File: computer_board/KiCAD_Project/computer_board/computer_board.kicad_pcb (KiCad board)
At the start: 4 copper layers, 101.6 x 33 mm, 43 parts, among them J1 Digitiziers, J2 Laser Driver, J3 Raspberry_Pi, Q1 BSS138, Q10 BSS138, Q11 BSS138, Q12 BSS138, Q2 BSS138, Q3 BSS138, Q4 BSS138, Q5 BSS138, Q6 BSS138, Q7 BSS138, Q8 BSS138, Q9 BSS138

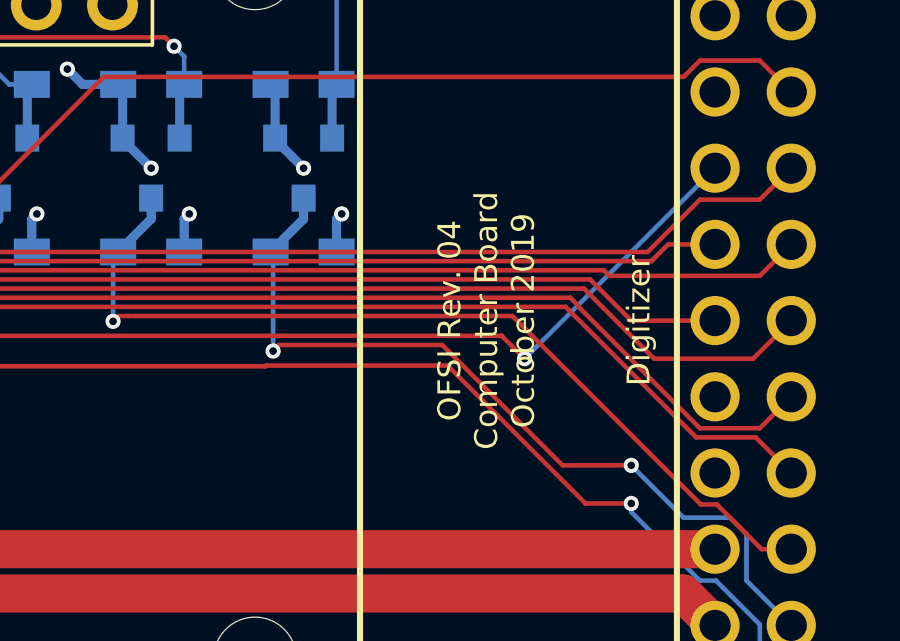
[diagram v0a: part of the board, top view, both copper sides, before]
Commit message: Change computer board to OFMI
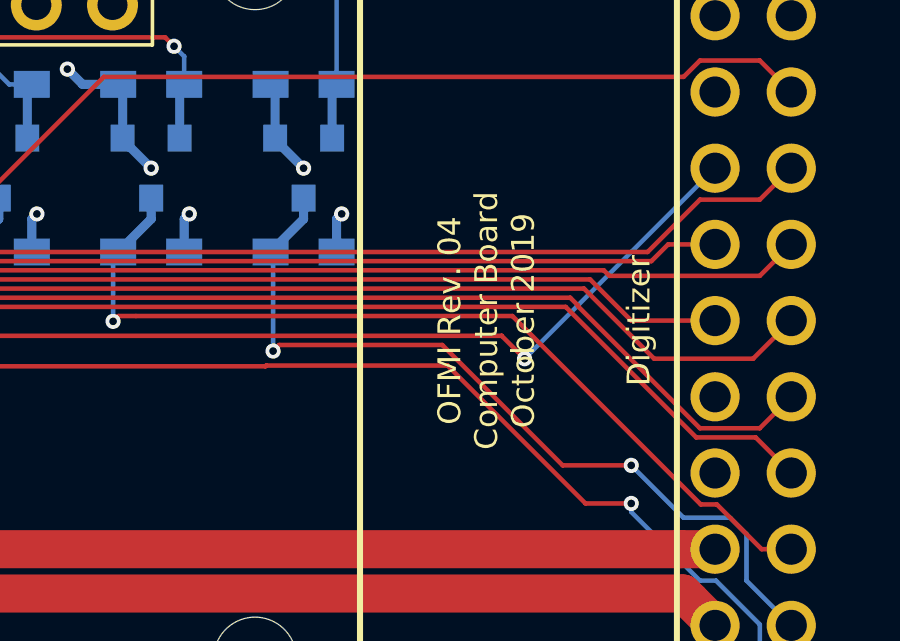
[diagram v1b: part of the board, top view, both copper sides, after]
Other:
- board text added: "OFMI Rev. 04 Computer Board October 2019"
- board text removed: "OFSI Rev. 04 Computer Board October 2019"
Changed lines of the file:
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@@
     (effects (font (size 0.762 0.762) (thickness 0.15)) (justify mirror))
   )
-  (gr_text "OFSI Rev. 04\nComputer Board\nOctober 2019" (at 173.99 72.39 90) (layer F.SilkS)
+  (gr_text "OFMI Rev. 04\nComputer Board\nOctober 2019" (at 173.99 72.39 90) (layer F.SilkS)
     (effects (font (size 0.762 0.762) (thickness 0.15)))
   )

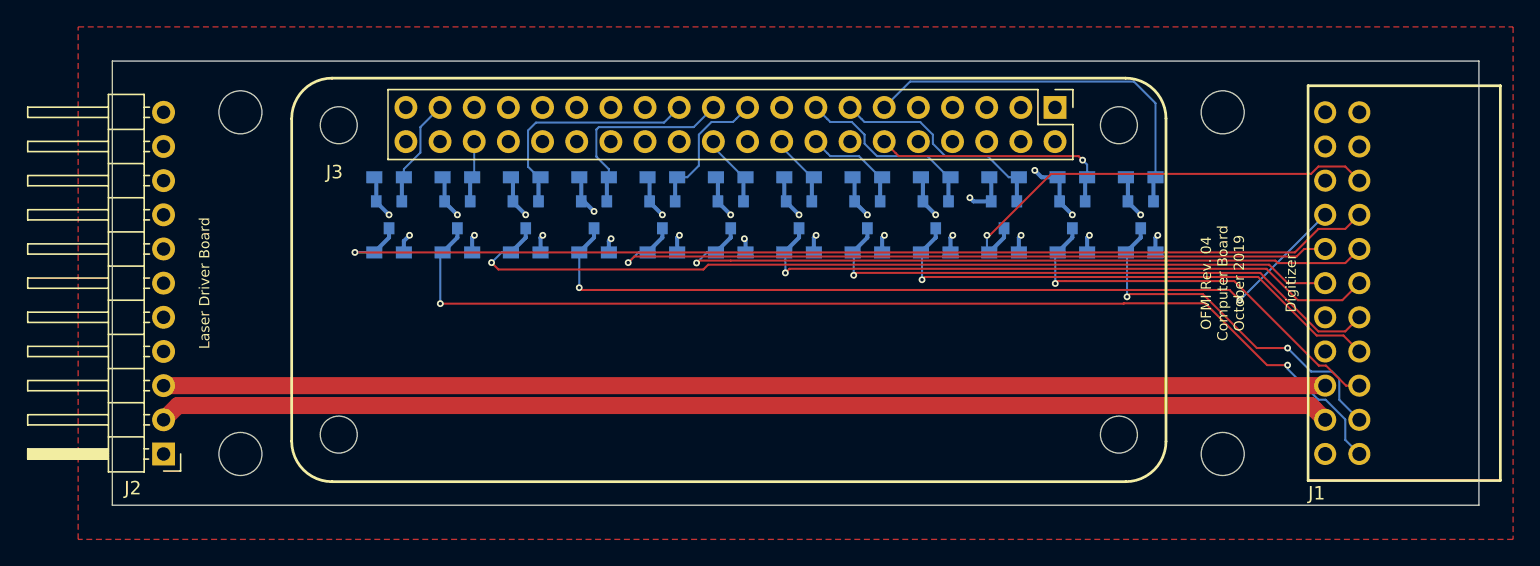
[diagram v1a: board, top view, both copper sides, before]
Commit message: Update computer board for rev 4.1
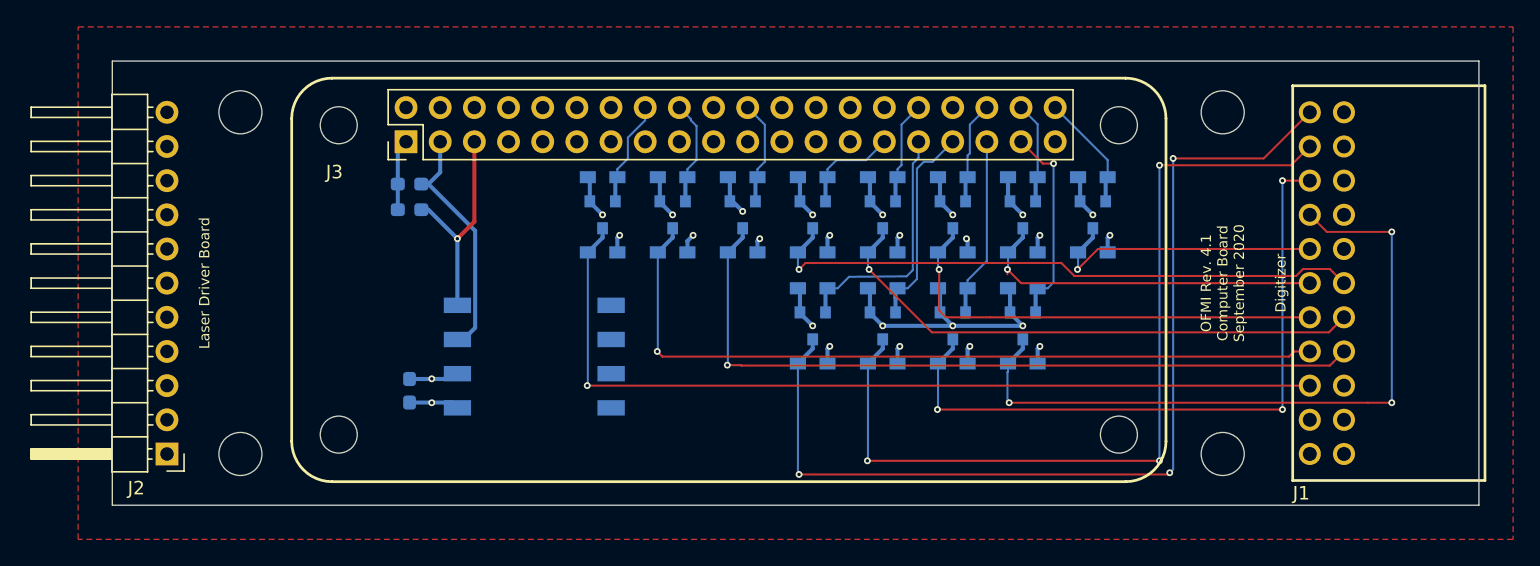
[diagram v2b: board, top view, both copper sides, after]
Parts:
- added C1: 0.1u, Capacitor_SMD:C_0603_1608Metric_Pad1.05x0.95mm_HandSolder, B.Cu at (113.5, 80.4)
- added R25: 1k, Resistor_SMD:R_0603_1608Metric_Pad1.05x0.95mm_HandSolder, B.Cu at (113.5, 65.0)
- added R26: 1k, Resistor_SMD:R_0603_1608Metric_Pad1.05x0.95mm_HandSolder, B.Cu at (113.5, 66.9)
- added U1: SSCMRNN015PA3A3, lib_fp:SSCMRN, B.Cu at (122.8, 77.9)
- moved Q9 29.8 mm to (127.9, 67.3)
- moved R17 29.8 mm to (127.9, 64.5)
- moved R21 29.8 mm to (127.9, 70.1)
- moved Q1 27.7 mm to (143.5, 75.6)
- moved R1 27.7 mm to (143.5, 72.8)
- moved R5 27.7 mm to (143.5, 78.4)
- moved Q12 21.3 mm to (143.5, 67.3)
- moved R20 21.3 mm to (143.5, 64.5)
- moved R24 21.3 mm to (143.5, 70.1)
- moved Q8 21.1 mm to (133.1, 67.3)
- moved R12 21.1 mm to (133.1, 64.5)
- moved R16 21.1 mm to (133.1, 70.1)
- moved Q2 20.9 mm to (148.7, 75.6)
- moved R2 20.9 mm to (148.7, 72.8)
- moved R6 20.9 mm to (148.7, 78.4)
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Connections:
- J1 pad 1: (no net) -> GND
- J1 pad 10: MOSI_5V -> MISO5_5V
- J1 pad 11: CS6_5V -> SCLK_5V
- J1 pad 12: SCLK_5V -> MISO6_5V
- J1 pad 13: CS5_5V -> MOSI_5V
- J1 pad 14: (no net) -> MISO7_5V
- J1 pad 15: CS4_5V -> CS_5V
- J1 pad 16: +5V -> MISO8_5V
- J1 pad 17: CS3_5V -> (no net)
- J1 pad 18: -12V -> MISO9_5V
- J1 pad 19: CS2_5V -> (no net)
- J1 pad 2: (no net) -> MISO1_5V
- J1 pad 20: +12V -> (no net)
- J1 pad 21: CS1_5V -> (no net)
- J1 pad 22: GND -> (no net)
- J1 pad 4: (no net) -> MISO2_5V
- J1 pad 5: CS9_5V -> (no net)
- J1 pad 6: (no net) -> MISO3_5V
- J1 pad 7: CS8_5V -> +5V
- J1 pad 8: MISO_5V -> MISO4_5V
- J1 pad 9: CS7_5V -> (no net)
- J2 pad 2: +12V -> (no net)
- J2 pad 3: -12V -> (no net)
- J2 pad 4: (no net) -> +5V
- J3 pad 11: CS2_3V3 -> (no net)
- J3 pad 12: CS3_3V3 -> (no net)
- J3 pad 13: CS9_3V3 -> (no net)
- J3 pad 15: CS4_3V3 -> (no net)
- J3 pad 16: CS5_3V3 -> MISO9_3V3
- J3 pad 18: CS6_3V3 -> MISO8_3V3
- J3 pad 19: MOSI_3V3 -> (no net)
- J3 pad 21: MISO_3V3 -> (no net)
- J3 pad 22: CS7_3V3 -> CS_3V3
- J3 pad 23: SCLK_3V3 -> (no net)
- J3 pad 29: (no net) -> SCLK_3V3
- J3 pad 3: (no net) -> SDA
- J3 pad 31: (no net) -> MISO1_3V3
- J3 pad 32: (no net) -> MOSI_3V3
- J3 pad 33: (no net) -> MISO2_3V3
- J3 pad 35: (no net) -> MISO3_3V3
- J3 pad 36: CS1_3V3 -> MISO7_3V3
- J3 pad 37: CS8_3V3 -> MISO4_3V3
- J3 pad 38: (no net) -> MISO6_3V3
- J3 pad 40: (no net) -> MISO5_3V3
- J3 pad 5: (no net) -> SCL
- Q1 pad 2: CS1_3V3 -> MISO1_3V3
- Q1 pad 3: CS1_5V -> MISO1_5V
- Q10 pad 2: MISO_3V3 -> CS_3V3
- Q10 pad 3: MISO_5V -> CS_5V
- Q2 pad 2: CS2_3V3 -> MISO2_3V3
- Q2 pad 3: CS2_5V -> MISO2_5V
- Q3 pad 2: CS3_3V3 -> MISO3_3V3
- Q3 pad 3: CS3_5V -> MISO3_5V
- Q4 pad 2: CS4_3V3 -> MISO4_3V3
- Q4 pad 3: CS4_5V -> MISO4_5V
- Q5 pad 2: CS5_3V3 -> MISO5_3V3
- Q5 pad 3: CS5_5V -> MISO5_5V
- Q6 pad 2: CS6_3V3 -> MISO6_3V3
- Q6 pad 3: CS6_5V -> MISO6_5V
- Q7 pad 2: CS7_3V3 -> MISO7_3V3
- Q7 pad 3: CS7_5V -> MISO7_5V
- Q8 pad 2: CS8_3V3 -> MISO8_3V3
- Q8 pad 3: CS8_5V -> MISO8_5V
- Q9 pad 2: CS9_3V3 -> MISO9_3V3
- Q9 pad 3: CS9_5V -> MISO9_5V
- R1 pad 2: CS1_3V3 -> MISO1_3V3
- R10 pad 2: CS6_3V3 -> MISO6_3V3
- R11 pad 2: CS7_3V3 -> MISO7_3V3
- R12 pad 2: CS8_3V3 -> MISO8_3V3
- R13 pad 2: CS5_5V -> MISO5_5V
- R14 pad 2: CS6_5V -> MISO6_5V
- R15 pad 2: CS7_5V -> MISO7_5V
- R16 pad 2: CS8_5V -> MISO8_5V
- R17 pad 2: CS9_3V3 -> MISO9_3V3
- R18 pad 2: MISO_3V3 -> CS_3V3
- R2 pad 2: CS2_3V3 -> MISO2_3V3
- R21 pad 2: CS9_5V -> MISO9_5V
- R22 pad 2: MISO_5V -> CS_5V
- R3 pad 2: CS3_3V3 -> MISO3_3V3
- R4 pad 2: CS4_3V3 -> MISO4_3V3
- R5 pad 2: CS1_5V -> MISO1_5V
- R6 pad 2: CS2_5V -> MISO2_5V
- R7 pad 2: CS3_5V -> MISO3_5V
- R8 pad 2: CS4_5V -> MISO4_5V
- R9 pad 2: CS5_3V3 -> MISO5_3V3
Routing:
- net +12V: track 87.2 -> 0.00 mm
- net -12V: track 86.4 -> 0.00 mm
- net CS1_5V: track 80.2 -> 0.00 mm, vias 2 -> 0
- net CS8_5V: track 79.5 -> 0.00 mm, vias 1 -> 0
- net MISO1_5V: track 0.00 -> 73.2 mm, vias 0 -> 3
- net MISO9_5V: track 0.00 -> 65.9 mm, vias 0 -> 1
- net MISO2_5V: track 0.00 -> 64.9 mm, vias 0 -> 3
- net MISO_5V: track 63.3 -> 0.00 mm, vias 2 -> 0
- net MISO8_5V: track 0.00 -> 58.5 mm, vias 0 -> 1
- net CS_5V: track 0.00 -> 56.9 mm, vias 0 -> 1
- net CS7_5V: track 53.9 -> 0.00 mm, vias 1 -> 0
- net MISO4_5V: track 0.00 -> 53.0 mm, vias 0 -> 3
- net MISO3_5V: track 0.00 -> 50.4 mm, vias 0 -> 3
- net CS6_5V: track 48.1 -> 0.00 mm, vias 1 -> 0
- net CS5_5V: track 43.9 -> 0.00 mm, vias 1 -> 0
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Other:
- board text added: "5V"
- board text added: "LG 3-0000048"
- board text added: "OFMI Rev. 4.1 Computer Board September 2020"
- board text removed: "LG 3-0000017"
- board text removed: "OFMI Rev. 04 Computer Board October 2019"

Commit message: Finalize computer board
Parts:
- removed the R1 at (143.5, 72.8)
- removed the R2 at (148.7, 72.8)
- added FID1: Fiducial, Fiducial:Fiducial_1mm_Mask3mm, B.Cu at (101.0, 78.7)
- added FID2: Fiducial, Fiducial:Fiducial_1mm_Mask3mm, B.Cu at (174.0, 64.8)
- added R25: 10k, Resistor_SMD:R_0603_1608Metric_Pad1.05x0.95mm_HandSolder, B.Cu at (148.7, 70.1)
- added R26: 10k, Resistor_SMD:R_0603_1608Metric_Pad1.05x0.95mm_HandSolder, B.Cu at (143.5, 70.1)
- R10, R11, R12, R13, R14, R15, R16, R17, R18, R19, R20, R21, R22, R23, R24, R3, R4, R5, R6, R7, R8, R9: footprint Resistors_SMD:R_0603_HandSoldering -> Resistor_SMD:R_0603_1608Metric_Pad1.05x0.95mm_HandSolder
- moved R17 26.6 mm to (153.9, 70.1), turned to 180 degrees
- moved R14 26.6 mm to (133.1, 64.5), turned to 0 degrees
- moved R12 26.0 mm to (159.1, 64.5)
- moved R16 26.0 mm to (159.1, 70.1)
- moved R21 21.6 mm to (148.7, 64.5), turned to 0 degrees
- moved R19 20.8 mm to (127.9, 64.5)
- moved R23 20.8 mm to (127.9, 70.1)
- moved R9 17.3 mm to (153.9, 78.4), turned to 180 degrees
- moved C1 17.1 mm to (130.0, 85.0), turned to 90 degrees
- moved R10 13.8 mm to (159.1, 78.4), turned to 180 degrees
- moved R5 11.8 mm to (153.9, 72.8), turned to 0 degrees
- moved R13 11.8 mm to (153.9, 64.5), turned to 0 degrees
- moved R6 11.8 mm to (159.1, 72.8), turned to 0 degrees
- moved R3 10.4 mm to (143.5, 72.8)
- moved R7 10.4 mm to (143.5, 78.4)
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- renumbered R25 to R1, R26 to R2
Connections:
- R10 pad 1: +3V3 -> +5V
- R10 pad 2: MISO6_3V3 -> MISO4_5V
- R11 pad 2: MISO7_3V3 -> MISO5_3V3
- R12 pad 2: MISO8_3V3 -> MISO6_3V3
- R13 pad 1: +5V -> +3V3
- R13 pad 2: MISO5_5V -> MISO7_3V3
- R14 pad 1: +5V -> +3V3
- R14 pad 2: MISO6_5V -> MISO8_3V3
- R15 pad 2: MISO7_5V -> MISO5_5V
- R16 pad 2: MISO8_5V -> MISO6_5V
- R17 pad 1: +3V3 -> +5V
- R17 pad 2: MISO9_3V3 -> MISO7_5V
- R18 pad 1: +3V3 -> +5V
- R18 pad 2: CS_3V3 -> MISO8_5V
- R19 pad 2: MOSI_3V3 -> MISO9_3V3
- R20 pad 2: SCLK_3V3 -> CS_3V3
- R21 pad 1: +5V -> +3V3
- R21 pad 2: MISO9_5V -> MOSI_3V3
- R22 pad 1: +5V -> +3V3
- R22 pad 2: CS_5V -> SCLK_3V3
- R23 pad 2: MOSI_5V -> MISO9_5V
- R24 pad 2: SCLK_5V -> CS_5V
- R3 pad 2: MISO3_3V3 -> MISO1_3V3
- R4 pad 2: MISO4_3V3 -> MISO2_3V3
- R5 pad 1: +5V -> +3V3
- R5 pad 2: MISO1_5V -> MISO3_3V3
- R6 pad 1: +5V -> +3V3
- R6 pad 2: MISO2_5V -> MISO4_3V3
- R7 pad 2: MISO3_5V -> MISO1_5V
- R8 pad 2: MISO4_5V -> MISO2_5V
- R9 pad 1: +3V3 -> +5V
- R9 pad 2: MISO5_3V3 -> MISO3_5V
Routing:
- net MISO4_5V: track 53.0 -> 26.8 mm, vias 3 -> 1
- net MISO1_5V: track 73.2 -> 47.6 mm, vias 3 -> 1
- net MISO2_5V: track 64.9 -> 41.1 mm, vias 3 -> 1
- net MISO3_5V: track 50.4 -> 34.8 mm, vias 3 -> 1
- net SCL: track 16.3 -> 27.9 mm
- net +3V3: track 58.3 -> 68.7 mm
- net SDA: track 17.8 -> 27.1 mm
- net CS_5V: track 56.9 -> 50.4 mm
- net MISO5_5V: track 21.4 -> 26.2 mm
- net SCLK_5V: track 45.3 -> 42.1 mm
- net MOSI_5V: track 41.3 -> 38.3 mm
- net MISO6_5V: track 26.8 -> 29.2 mm
- net MISO7_5V: track 34.4 -> 36.5 mm
- net MISO8_5V: track 58.5 -> 60.0 mm
- net MISO9_5V: track 65.9 -> 67.0 mm
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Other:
- board text added: "CS"
- board text added: "MISO1"
- board text added: "MISO2"
- board text added: "MISO3"
- board text added: "MISO4"
- board text added: "MISO5"
- board text added: "MISO6"
- board text added: "MISO7"
- board text added: "MISO8"
- board text added: "MISO9"
- board text removed: "+12"
- board text removed: "-12"
- board text removed: "CS1"
- board text removed: "CS2"
- board text removed: "CS3"
- board text removed: "CS4"
- board text removed: "CS5"
- board text removed: "CS6"
- board text removed: "CS7"
- board text removed: "CS8"
- board text removed: "CS9"
- board text removed: "MISO"
